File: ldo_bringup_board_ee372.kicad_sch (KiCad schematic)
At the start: 53 parts, among them J1 VIN, J2 GND, J3 IBIAS, J4 VOUT, J5 VIN_SMA, J6 VOUT_SMA, J7 GND, Q1 FDV305N, Q2 FDV305N, Q3 FDV305N, Q4 FDV305N, Q5 FDV305N, SW1 SW_SPDT, U1 LDO_DualMode_BGR_EE372

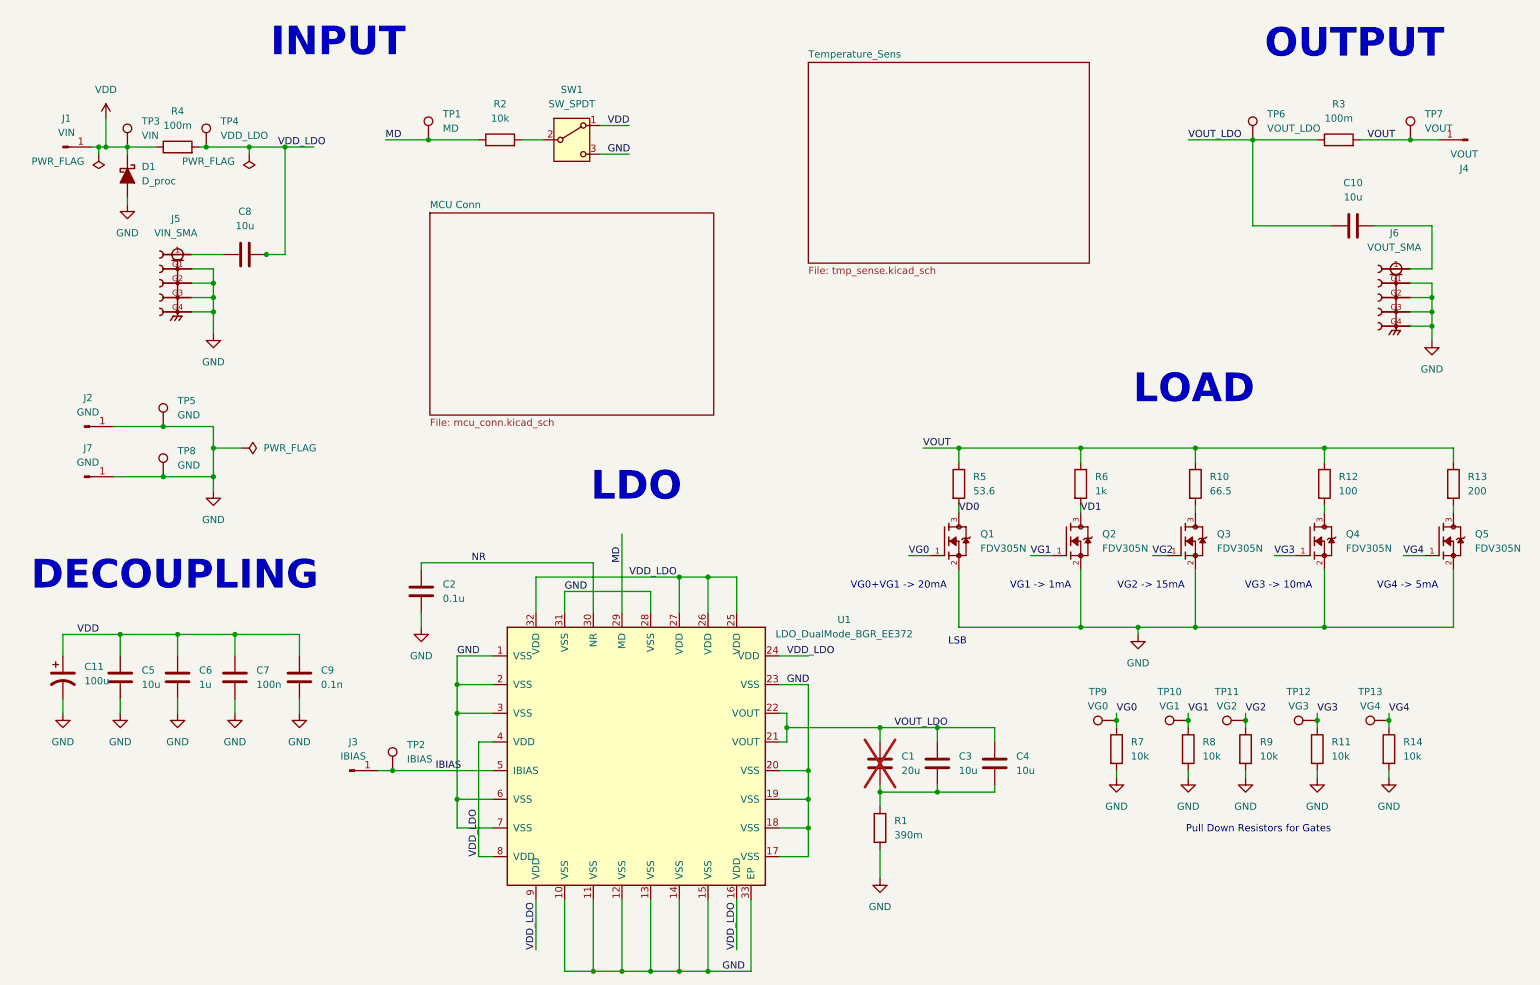
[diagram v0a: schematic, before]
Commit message: Join the gate and mode nets across sheets with global labels
VG0 to VG4 and MD now use global labels on both sheets, so the MCU
header reaches the FET gates and the MD pin. Nets go from 35 to 29
because each pair merged into one.

Adds R17, a gate pull-down for Q6 on the MCU sheet, with no value or
footprint yet. 66 parts.

The MCU sheet's VDD label is still local, so R16 is not on the VDD rail.
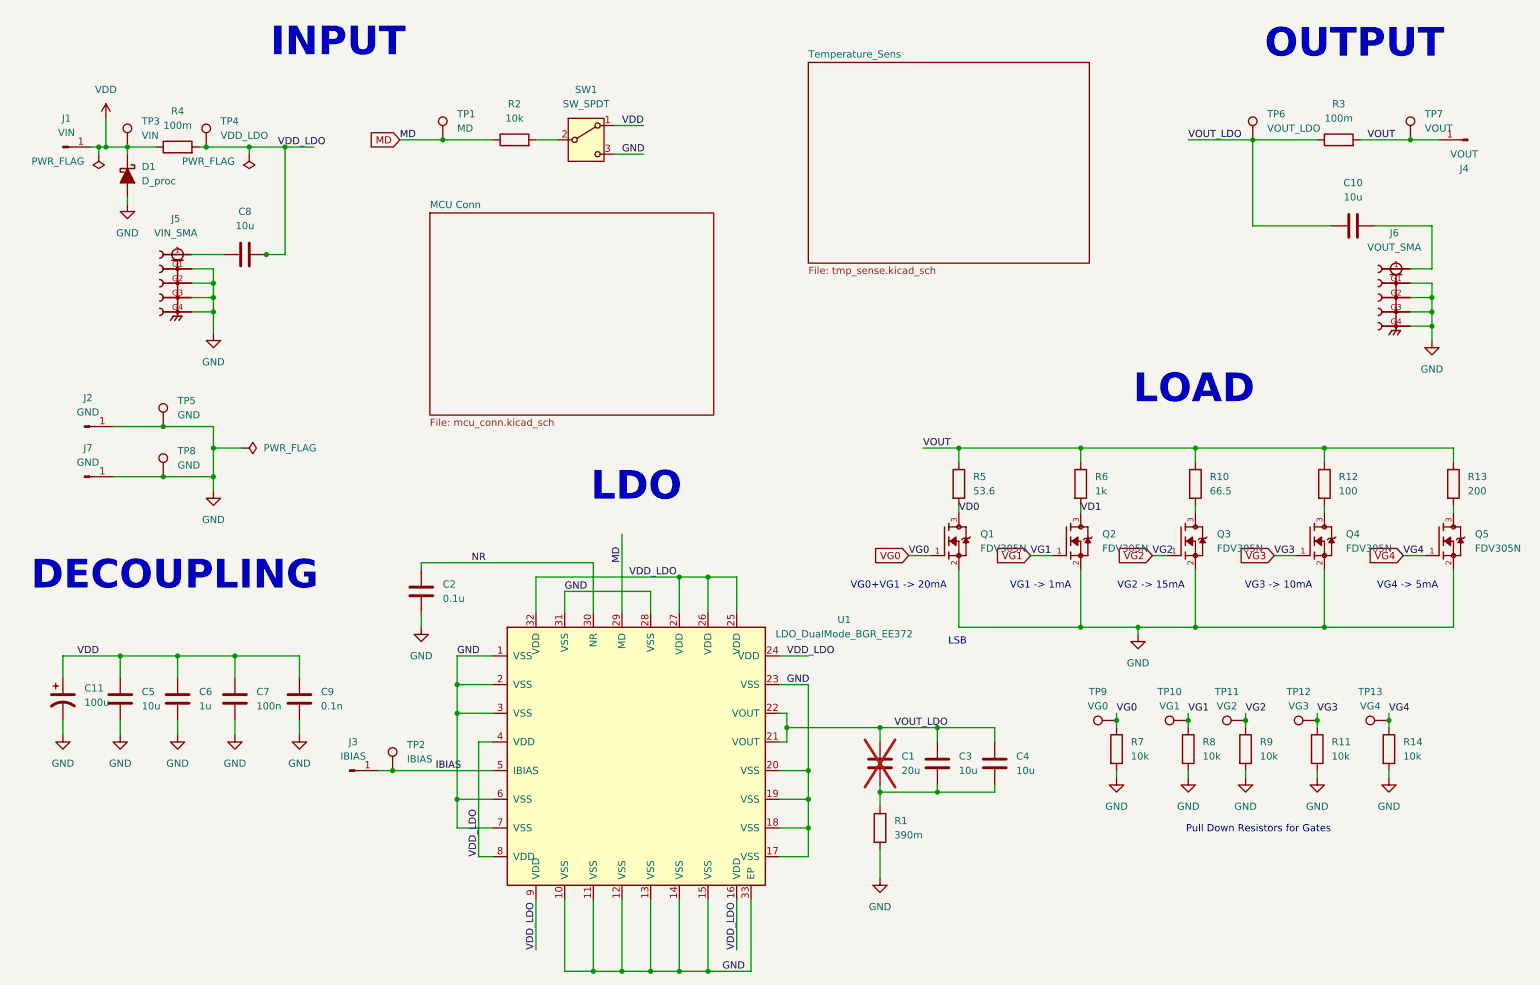
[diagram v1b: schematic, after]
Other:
- moved on the sheet: C11, C5, C6, C7, C9, R2, SW1, TP1
